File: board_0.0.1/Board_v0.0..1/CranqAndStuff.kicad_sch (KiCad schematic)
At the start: 14 parts, among them U2 MAX9926UAEE+

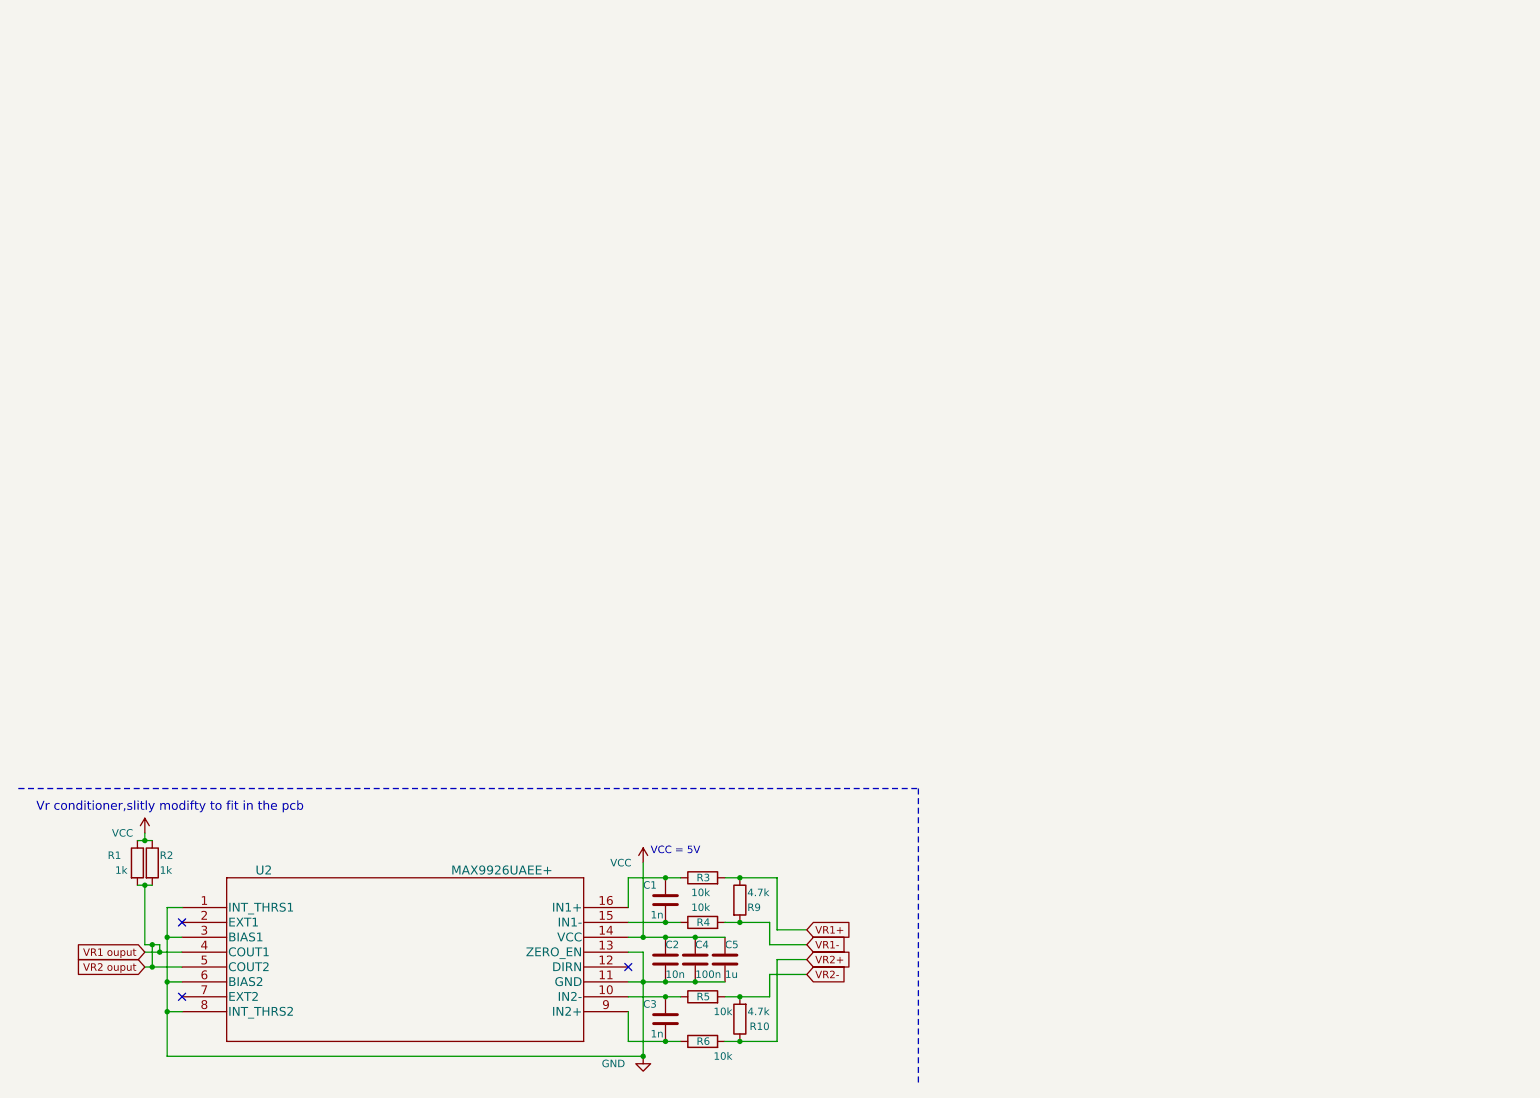
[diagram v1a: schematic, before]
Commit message: new VR conditioner that should work wis honda
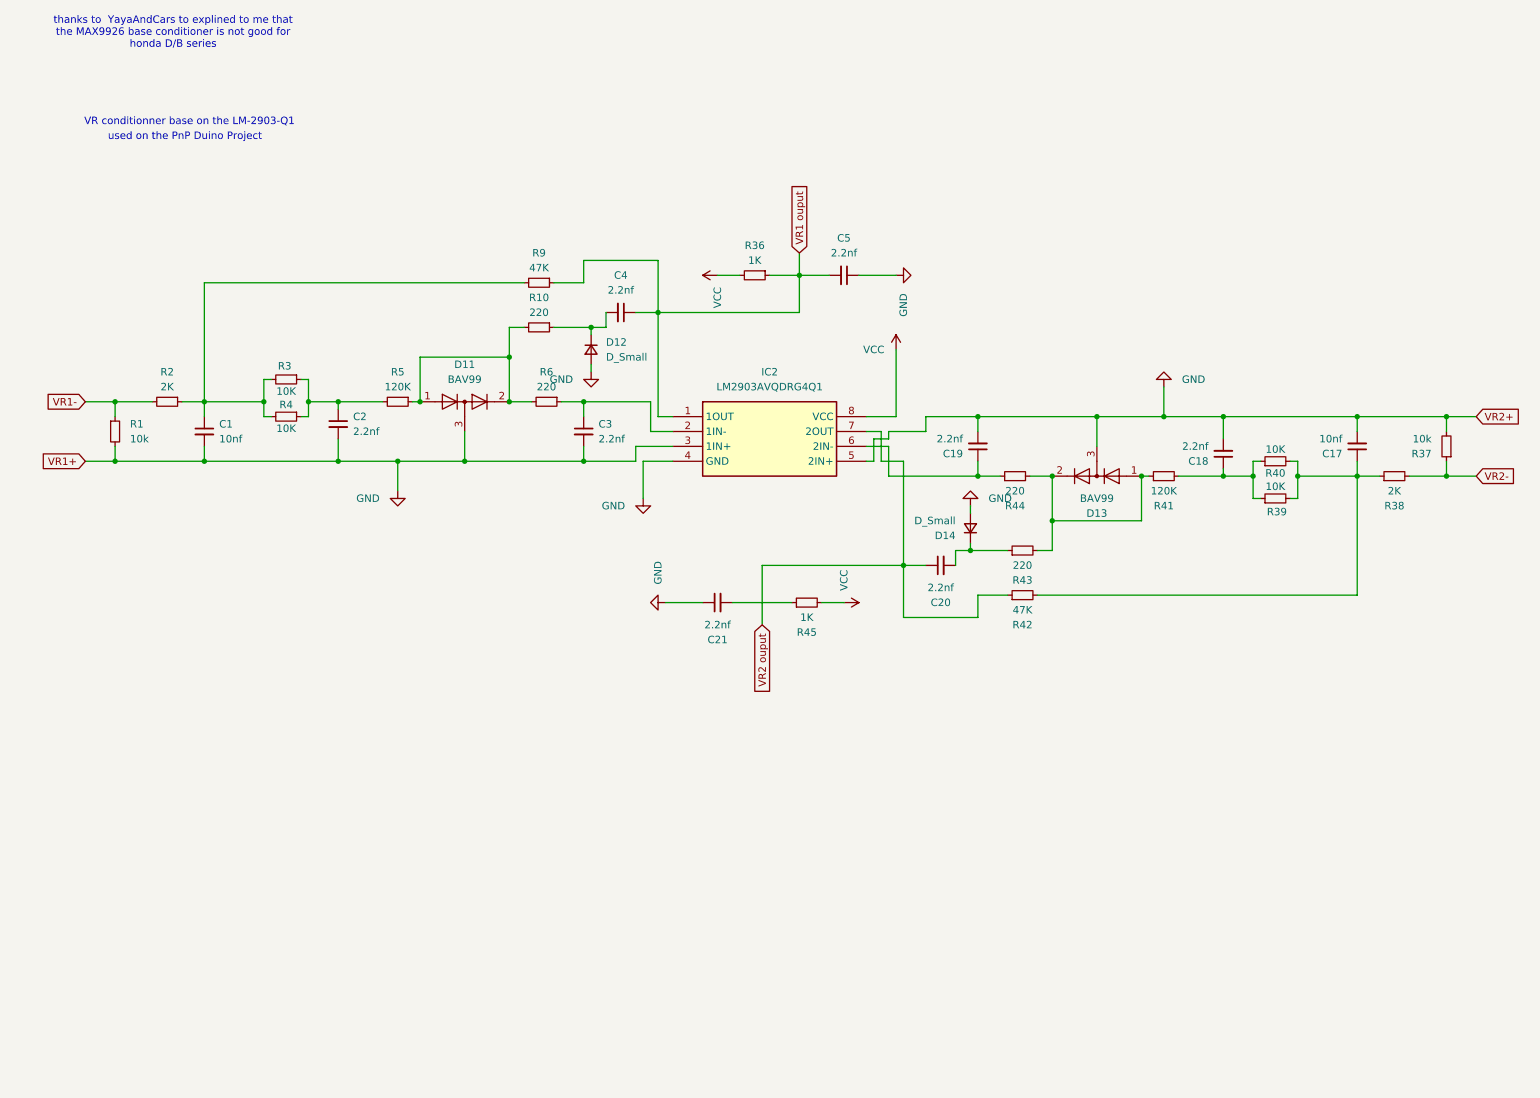
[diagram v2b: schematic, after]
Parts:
- removed C1, C3: 1n, Capacitor_SMD:C_0603_1608Metric, symbol Device:C
- removed C2: 10n, Capacitor_SMD:C_0603_1608Metric, symbol Device:C
- removed C4: 100n, Capacitor_SMD:C_0603_1608Metric, symbol Device:C
- removed C5: 1u, Capacitor_SMD:C_0603_1608Metric, symbol Device:C
- removed R1, R2: 1k, Resistor_SMD:R_0603_1608Metric_Pad1.05x0.95mm_HandSolder, symbol Device:R
- removed R10, R9: 4.7k, Resistor_THT:R_Axial_DIN0207_L6.3mm_D2.5mm_P7.62mm_Horizontal, symbol Device:R
- removed R3, R4, R5, R6: 10k, Resistor_SMD:R_1206_3216Metric, symbol Device:R
- removed U2: MAX9926UAEE+, MAX9926UAEE+:MAX9926UAEE&plus_, symbol 2021-02-17_17-37-40:MAX9926UAEE+
- added C1, C17: 10nf, symbol Device:C_Small
- added C18, C19, C2, C20, C21, C3, C4, C5: 2.2nf, symbol Device:C_Small
- added D11, D13: BAV99, Package_TO_SOT_SMD:SOT-23, symbol Diode:BAV99
- added D12, D14: D_Small, symbol Device:D_Small
- added IC2: LM2903AVQDRG4Q1, SOIC127P600X175-8N, symbol LM2903AVQDRG4Q1:LM2903AVQDRG4Q1
- added R1, R37: 10k, symbol Device:R_Small
- added R10, R43, R44, R6: 220, symbol Device:R_Small
- added R2, R38: 2K, symbol Device:R_Small
- added R3, R39, R4, R40: 10K, symbol Device:R_Small
- added R36, R45: 1K, symbol Device:R_Small
- added R41, R5: 120K, symbol Device:R_Small
- added R42, R9: 47K, symbol Device:R_Small
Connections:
- net GND: now also C1.2, C17.2, C18.2, C19.2, C2.2, C21.1, C3.2, C5.1, D11.3 (K), D12.2 (A), D13.3 (K), D14.2 (A), IC2.3 (1IN+), IC2.4 (GND), IC2.5 (2IN+), R1.2, R37.2
- net VCC: now also IC2.8 (VCC), R36.2, R45.2
- net VR1 ouput: now also C4.1, C5.2, IC2.1 (1OUT), R36.1, R9.1
- net VR1-: now also R1.1, R2.2
- net VR2-: now also R37.1, R38.2
- new net: C3.1, IC2.2 (1IN-), R6.1
- new net: C19.1, IC2.6 (2IN-), R44.1
- new net: C18.1, R39.1, R40.1, R41.2
- new net: D11.1 (K), D11.2 (A), R10.2, R5.1, R6.2
- new net: C2.1, R3.1, R4.1, R5.2
- new net: D13.1 (K), D13.2 (A), R41.1, R43.2, R44.2
- new net: C21.2, R45.1
- new net: C17.1, R38.1, R39.2, R40.2, R42.2
- new net: C4.2, D12.1 (K), R10.1
- new net: C1.1, R2.1, R3.2, R4.2, R9.2
- new net: C20.2, D14.1 (K), R43.1
- new net VR2 ouput: C20.1, IC2.7 (2OUT), R42.1
- no-connect marks 3 -> 0
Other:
- note added: "VR conditionner base on the LM-2903-Q1"
- note added: "thanks to YayaAndCars to explined to me that the MAX9926 base conditioner is not good for honda D/B series"
- note added: "used on the PnP Duino Project"
- note removed: "VCC = 5V"
- note removed: "Vr conditioner,slitly modifty to fit in the pcb"
